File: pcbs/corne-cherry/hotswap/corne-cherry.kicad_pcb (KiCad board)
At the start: 2 copper layers, 277.2 x 107.5 mm, 180 parts, among them J1 TYPE-C-31-M-13C, J2 TRS, J3 Conn_01x04, J4 Conn_01x03, SW1 SW_Push, SW10 SW_Push, SW11 SW_Push, SW12 SW_Push, SW13 SW_Push, SW14 SW_Push, SW15 SW_Push, SW16 SW_Push, SW17 SW_Push, SW18 SW_Push, SW19 SW_Push, SW2 SW_Push, SW20 SW_Push, SW21 SW_Push, SW3 SW_Push, SW4 SW_Push, SW5 SW_Push, SW6 SW_Push, SW7 SW_Push, SW8 SW_Push, SW9 SW_Push, U1 RP2040, U2 NCP1117LPST33T3G, U3 TPD4E05U06DQAR, U4 W25Q128JVSIQ, Y1 12MHz 18pF

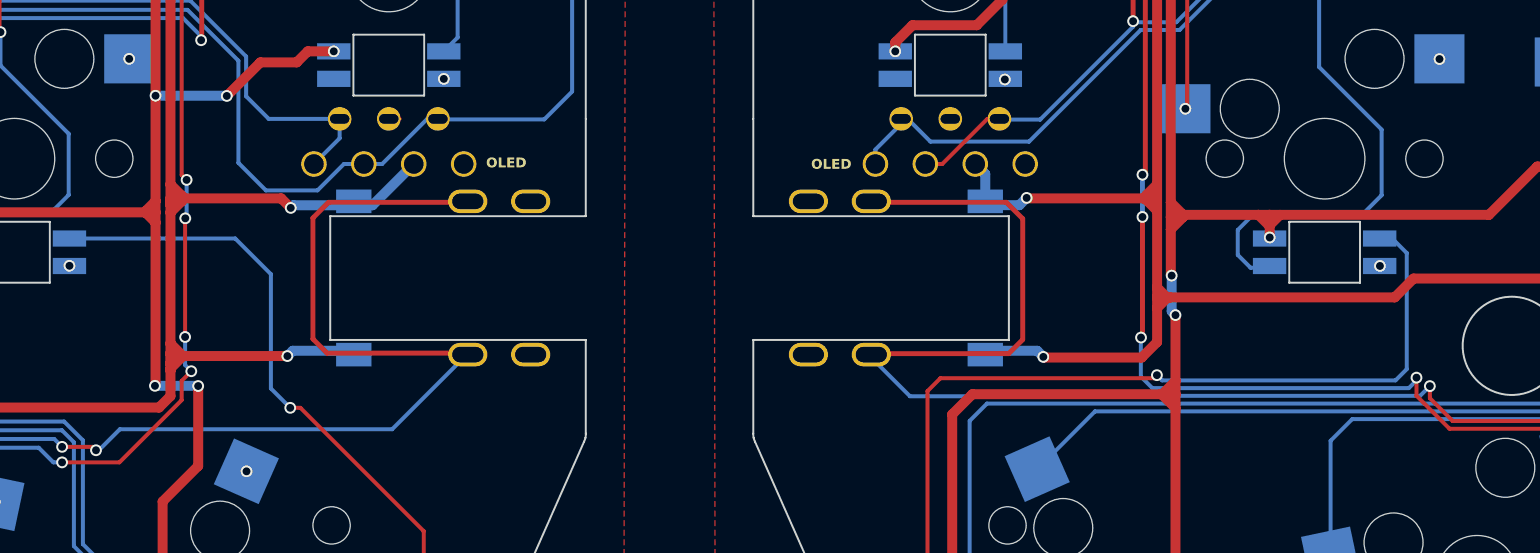
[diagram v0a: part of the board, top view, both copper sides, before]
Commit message: Add USB C port to replace TRS jack
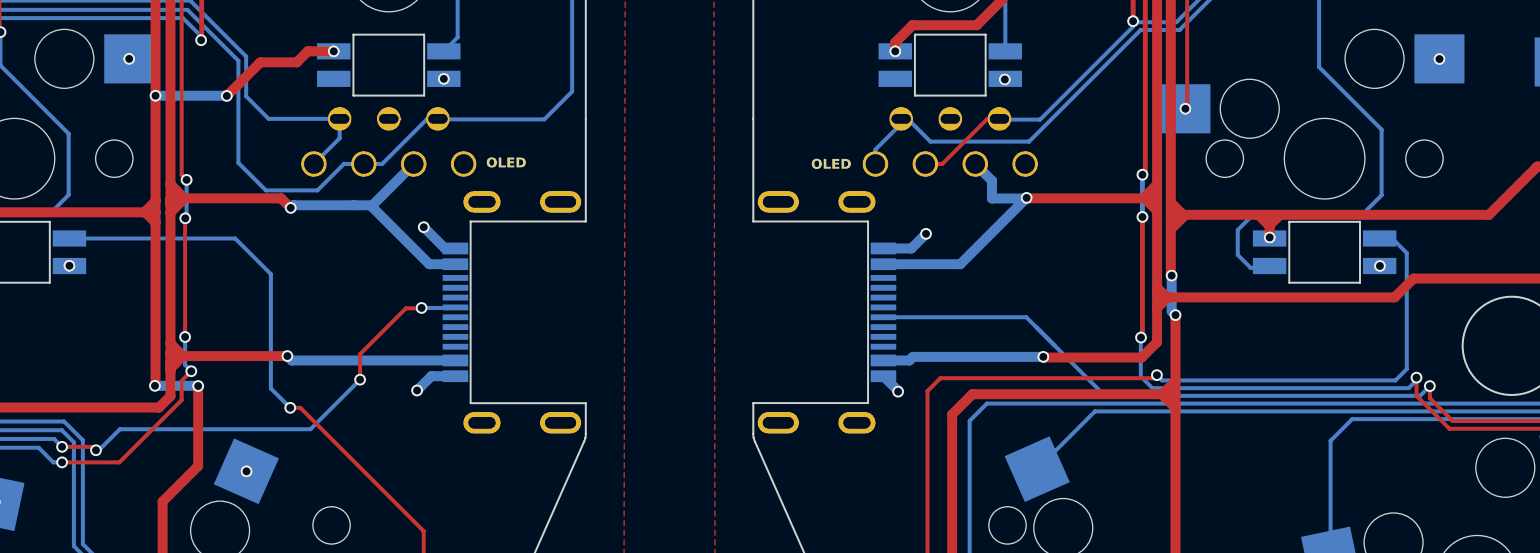
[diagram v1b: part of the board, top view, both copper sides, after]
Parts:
- J2, rJ2: value TRS -> TYPE-C-31-M-13C; footprint kbd_local:PJ-398A-5A_PJ-399B-6A -> kbd:TYPE-C-31-M-13C
- moved J2 2.17 mm to (-5.54, 36.4), turned to -90 degrees
- moved rJ2 2.16 mm to (5.54, 36.4), turned to 90 degrees
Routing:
- net /left/TX: track 88.9 -> 67.5 mm, vias 2 -> 4
- net /right/TX: track 95.8 -> 75.1 mm
- net +5VR: track 110.8 -> 123.6 mm
- net +5V: track 114.1 -> 123.8 mm
- net GND: track 43.5 -> 47.8 mm, vias 69 -> 71
- net GNDR: track 91.7 -> 95.3 mm, vias 71 -> 73
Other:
- outline, holes or cut-outs redrawn

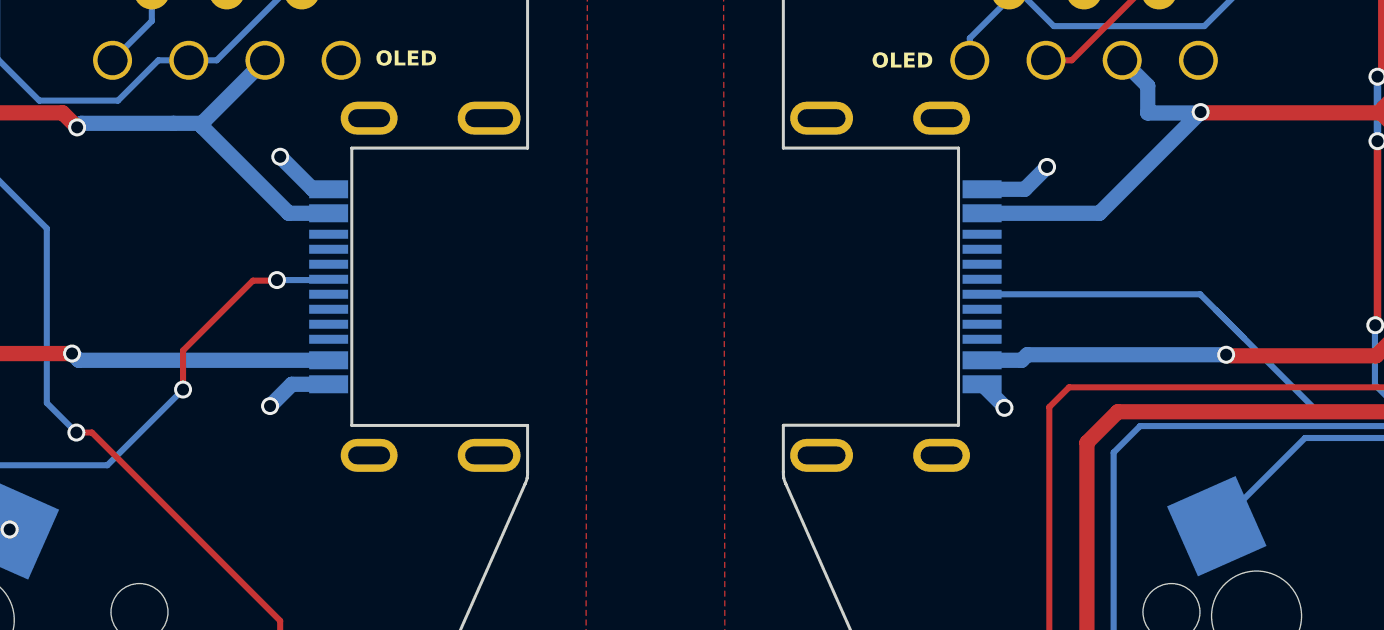
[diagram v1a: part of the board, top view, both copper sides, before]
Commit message: Fix some connections
Also connect the other USB D+ pin to the controller.
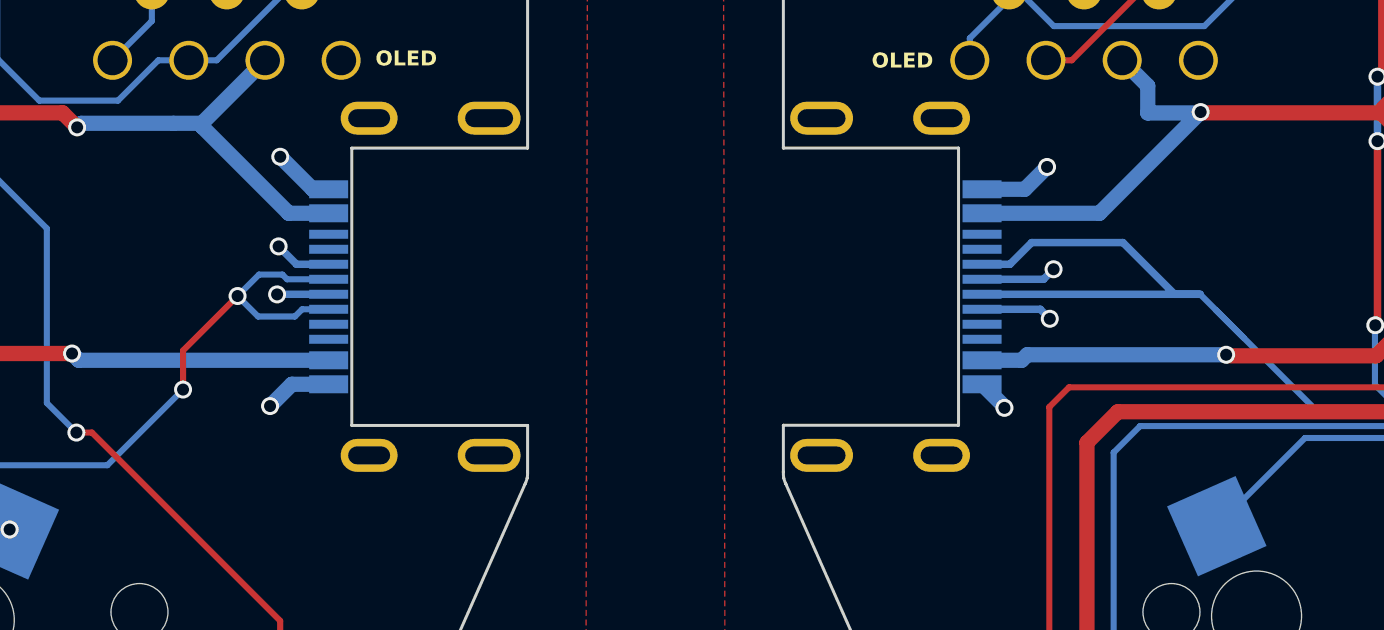
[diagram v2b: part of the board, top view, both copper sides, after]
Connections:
- J2 pad A7: unconnected-(J2-D--PadA7) -> GND
- J2 pad B6: unconnected-(J2-D+-PadB6) -> /left/TX
- J2 pad B7: unconnected-(J2-D--PadB7) -> GND
- rJ2 pad A7: unconnected-(rJ2-D--PadA7) -> GNDR
- rJ2 pad B6: unconnected-(rJ2-D+-PadB6) -> /right/TX
- rJ2 pad B7: unconnected-(rJ2-D--PadB7) -> GNDR
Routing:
- net /right/TX: track 75.1 -> 83.4 mm
- net GNDR: track 95.3 -> 100.2 mm, vias 73 -> 75
- net GND: track 47.8 -> 51.4 mm, vias 71 -> 73
- net /left/TX: track 67.5 -> 71.0 mm
